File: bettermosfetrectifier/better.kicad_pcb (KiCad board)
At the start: 2 copper layers, 20 parts, among them IC1 LT4322RMS8#PBF, IC2 LT4322RMS8#PBF, IC3 LT4322RMS8#PBF, IC4 LT4322RMS8#PBF, IC5 LT4322RMS8#PBF, IC6 LT4322RMS8#PBF, J1 Conn_01x02, J2 Conn_01x03, Q1 IRFS7430-7P, Q2 IRFS7430-7P, Q3 IRFS7430-7P, Q4 IRFS7430-7P, Q5 IRFS7430-7P, Q6 IRFS7430-7P

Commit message: Add files via upload
Added depletion mode mosfets and added capacitors on power mosfet gates
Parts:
- added C1: 10nF, Capacitor_SMD:C_0603_1608Metric, F.Cu at (90.5, 91.3)
- added C2: 10nF, Capacitor_SMD:C_0603_1608Metric, F.Cu at (90.5, 93.8)
- added C3: 10nF, Capacitor_SMD:C_0603_1608Metric, F.Cu at (90.5, 96.3)
- added C4: 10nF, Capacitor_SMD:C_0603_1608Metric, F.Cu at (90.5, 98.8)
- added C5: 10nF, Capacitor_SMD:C_0603_1608Metric, F.Cu at (90.5, 101.3)
- added C6: 10nF, Capacitor_SMD:C_0603_1608Metric, F.Cu at (90.5, 103.8)
- added Q10: DN3135, Library:SOT-89_3MC_MCH, F.Cu at (104.1, 76.4)
- added Q11: DN3135, Library:SOT-89_3MC_MCH, F.Cu at (110.4, 76.4)
- added Q12: DN3135, Library:SOT-89_3MC_MCH, F.Cu at (116.7, 76.4)
- added Q7: DN3135, Library:SOT-89_3MC_MCH, F.Cu at (104.0, 70.5)
- added Q8: DN3135, Library:SOT-89_3MC_MCH, F.Cu at (110.2, 70.5)
- added Q9: DN3135, Library:SOT-89_3MC_MCH, F.Cu at (116.5, 70.5)
- CVDDA1, CVDDA2, CVDDA3, CVDDA4, CVDDA5, CVDDA6: footprint Capacitor_SMD:C_0201_0603Metric -> Capacitor_SMD:C_0603_1608Metric
- moved Q1 46.1 mm to (72.4, 49.0), turned to 0 degrees
- moved Q6 30.1 mm to (70.9, 104.5)
- moved CVDDA2 28.8 mm to (90.7, 65.0)
- moved CVDDA1 26.9 mm to (90.8, 69.5)
- moved Q2 26.5 mm to (72.0, 35.5), turned to 0 degrees
- moved Q5 23.7 mm to (71.0, 91.0)
- moved Q4 17.1 mm to (71.4, 77.5)
- moved CVDDA6 11.6 mm to (90.5, 85.5)
- moved Q3 11.1 mm to (71.8, 63.5)
- moved CVDDA5 8.01 mm to (90.5, 82.0)
- moved CVDDA4 3.39 mm to (90.7, 78.0)
- moved IC3 2.42 mm to (98.8, 49.4)
- moved IC4 2.42 mm to (98.8, 54.0)
- moved IC5 2.42 mm to (98.8, 58.7)
- moved IC6 2.42 mm to (98.8, 63.3)
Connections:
- CVDDA2 pad 1: Net-(IC1-CATHODE) -> Net-(J2-Pin_1)
- CVDDA3 pad 1: Net-(IC4-CATHODE) -> Net-(J2-Pin_2)
- CVDDA5 pad 1: Net-(IC6-CATHODE) -> Net-(J2-Pin_3)
- IC3 pad 5: Net-(IC2-CATHODE) -> Net-(IC3-CATHODE)
- IC3 pad 8: Net-(IC2-CATHODE) -> Net-(IC3-CATHODE)
- IC5 pad 5: Net-(IC2-CATHODE) -> Net-(IC5-CATHODE)
- IC5 pad 8: Net-(IC2-CATHODE) -> Net-(IC5-CATHODE)
- J1 pad 1: Net-(IC2-CATHODE) -> Net-(J1-Pin_1)
- J2 pad 1: Net-(IC1-CATHODE) -> Net-(J2-Pin_1)
- J2 pad 2: Net-(IC4-CATHODE) -> Net-(J2-Pin_2)
- J2 pad 3: Net-(IC6-CATHODE) -> Net-(J2-Pin_3)
- Q1 pad 4: Net-(IC1-CATHODE) -> Net-(J2-Pin_1)
- Q2 pad 2: Net-(IC1-CATHODE) -> Net-(J2-Pin_1)
- Q2 pad 3: Net-(IC1-CATHODE) -> Net-(J2-Pin_1)
- Q2 pad 4: Net-(IC2-CATHODE) -> Net-(J1-Pin_1)
- Q2 pad 5: Net-(IC1-CATHODE) -> Net-(J2-Pin_1)
- Q2 pad 6: Net-(IC1-CATHODE) -> Net-(J2-Pin_1)
- Q3 pad 2: Net-(IC4-CATHODE) -> Net-(J2-Pin_2)
- Q3 pad 3: Net-(IC4-CATHODE) -> Net-(J2-Pin_2)
- Q3 pad 4: Net-(IC2-CATHODE) -> Net-(J1-Pin_1)
- Q3 pad 5: Net-(IC4-CATHODE) -> Net-(J2-Pin_2)
- Q3 pad 6: Net-(IC4-CATHODE) -> Net-(J2-Pin_2)
- Q4 pad 4: Net-(IC4-CATHODE) -> Net-(J2-Pin_2)
- Q5 pad 2: Net-(IC6-CATHODE) -> Net-(J2-Pin_3)
- Q5 pad 3: Net-(IC6-CATHODE) -> Net-(J2-Pin_3)
- Q5 pad 4: Net-(IC2-CATHODE) -> Net-(J1-Pin_1)
- Q5 pad 5: Net-(IC6-CATHODE) -> Net-(J2-Pin_3)
- Q5 pad 6: Net-(IC6-CATHODE) -> Net-(J2-Pin_3)
- Q6 pad 4: Net-(IC6-CATHODE) -> Net-(J2-Pin_3)

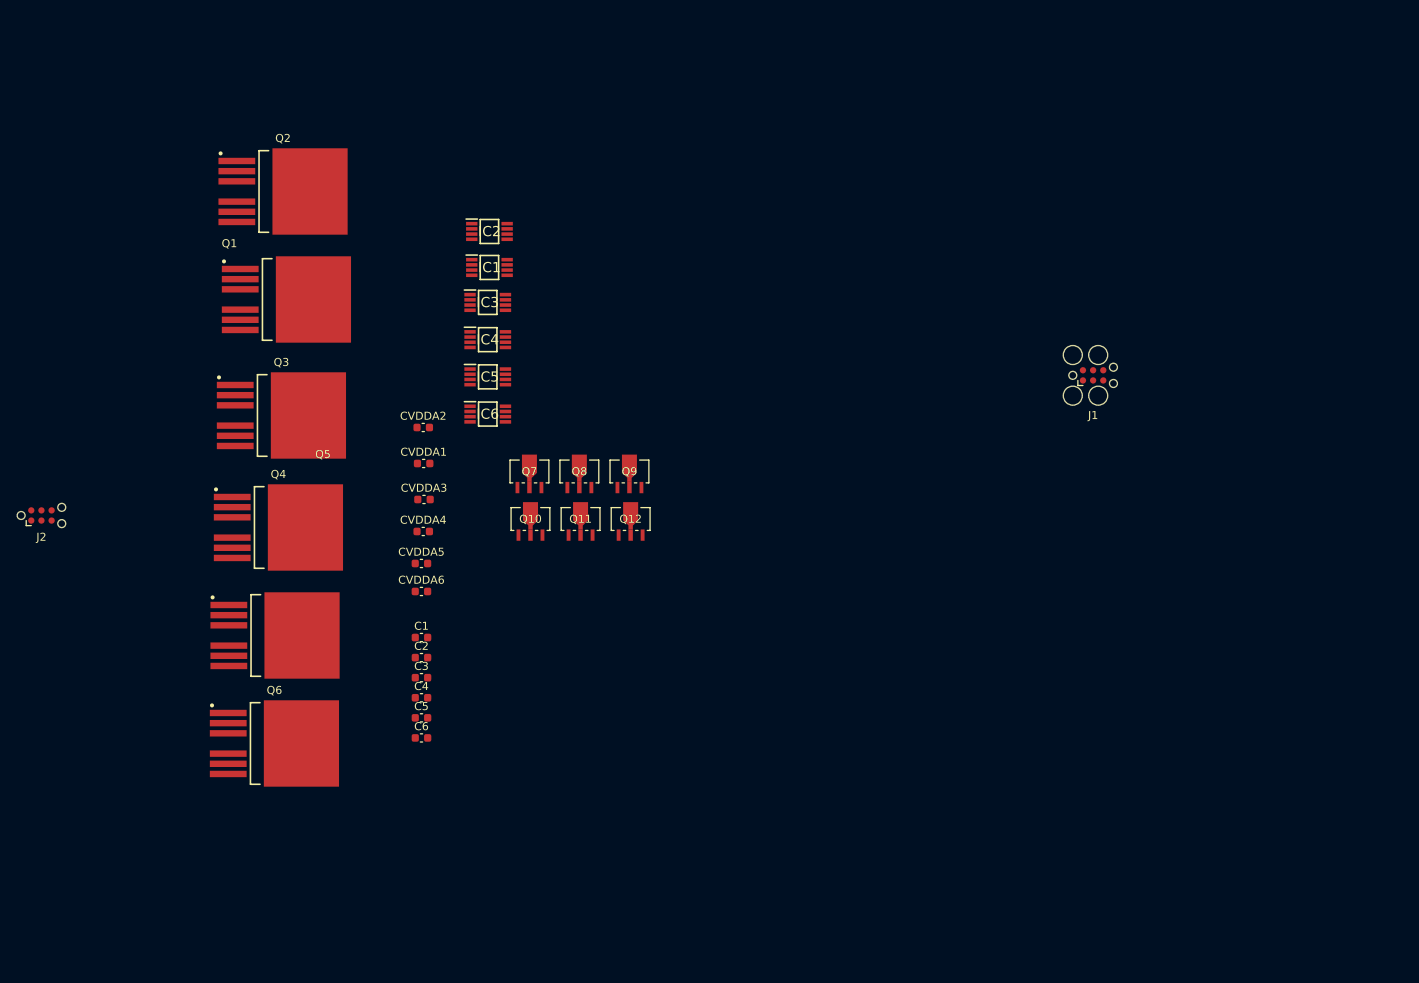
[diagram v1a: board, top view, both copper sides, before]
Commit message: Goon
Changed mosfets to 100V 16A ones (old ones were 40V 240A), added footprints to capacitors and terminals
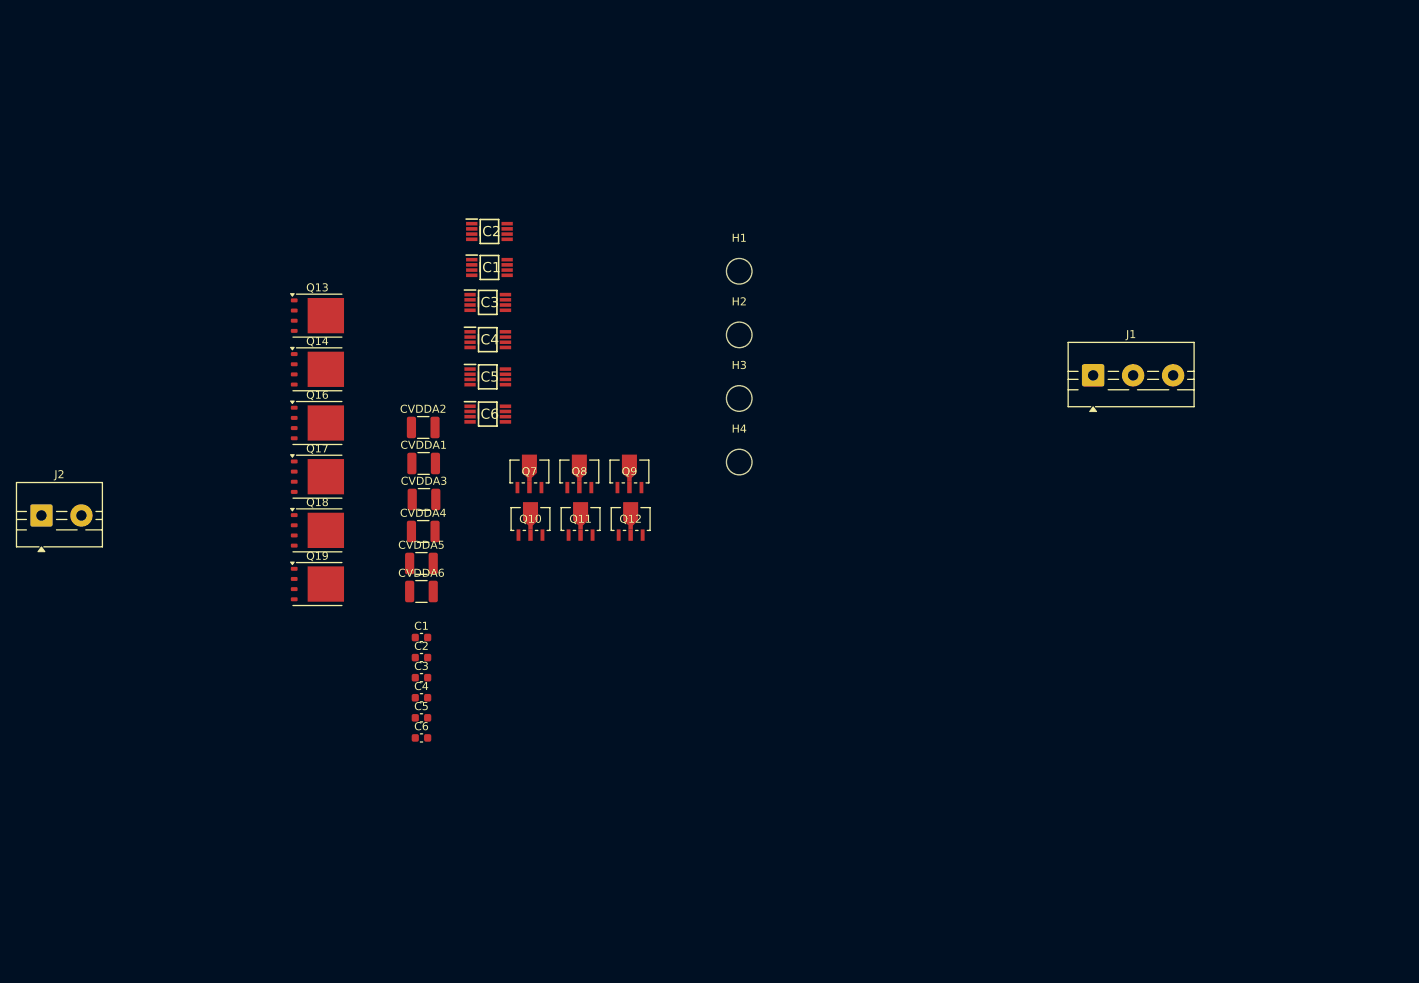
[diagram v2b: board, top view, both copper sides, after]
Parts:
- removed Q1, Q2, Q3, Q4, Q5, Q6: IRFS7430-7P, TO127P1524X508-8_7N-V1:TO127P1524X508-8_7N
- added H1: MountingHole, MountingHole:MountingHole_3.2mm_M3, F.Cu at (130.2, 45.5)
- added H2: MountingHole, MountingHole:MountingHole_3.2mm_M3, F.Cu at (130.2, 53.4)
- added H3: MountingHole, MountingHole:MountingHole_3.2mm_M3, F.Cu at (130.2, 61.4)
- added H4: MountingHole, MountingHole:MountingHole_3.2mm_M3, F.Cu at (130.2, 69.3)
- added Q13: BSC050N10NS5ATMA1, Package_TO_SOT_SMD:TDSON-8-1, F.Cu at (77.5, 51.0)
- added Q14: BSC050N10NS5ATMA1, Package_TO_SOT_SMD:TDSON-8-1, F.Cu at (77.5, 57.7)
- added Q16: BSC050N10NS5ATMA1, Package_TO_SOT_SMD:TDSON-8-1, F.Cu at (77.5, 64.4)
- added Q17: BSC050N10NS5ATMA1, Package_TO_SOT_SMD:TDSON-8-1, F.Cu at (77.5, 71.2)
- added Q18: BSC050N10NS5ATMA1, Package_TO_SOT_SMD:TDSON-8-1, F.Cu at (77.5, 77.9)
- added Q19: BSC050N10NS5ATMA1, Package_TO_SOT_SMD:TDSON-8-1, F.Cu at (77.5, 84.6)
- CVDDA1, CVDDA2, CVDDA3, CVDDA4, CVDDA5, CVDDA6: footprint Capacitor_SMD:C_0603_1608Metric -> Capacitor_SMD:C_1210_3225Metric
- J1: footprint Connector:Tag-Connect_TC2030-IDC-FP_2x03_P1.27mm_Vertical -> TerminalBlock:TerminalBlock_MaiXu_MX126-5.0-03P_1x03_P5.00mm
- J2: footprint Connector:Tag-Connect_TC2030-IDC-NL_2x03_P1.27mm_Vertical -> TerminalBlock:TerminalBlock_MaiXu_MX126-5.0-02P_1x02_P5.00mm
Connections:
- C1 pad 2: Net-(J2-Pin_1) -> Net-(IC2-ANODE)
- C2 pad 1: Net-(J1-Pin_2) -> Net-(IC1-ANODE)
- C3 pad 2: Net-(J2-Pin_2) -> Net-(IC3-ANODE)
- C4 pad 1: Net-(J1-Pin_2) -> Net-(IC1-ANODE)
- C5 pad 2: Net-(J2-Pin_3) -> Net-(IC5-ANODE)
- C6 pad 1: Net-(J1-Pin_2) -> Net-(IC1-ANODE)
- CVDDA1 pad 1: Net-(J1-Pin_2) -> Net-(IC1-ANODE)
- CVDDA2 pad 1: Net-(J2-Pin_1) -> Net-(IC2-ANODE)
- CVDDA3 pad 1: Net-(J2-Pin_2) -> Net-(IC3-ANODE)
- CVDDA4 pad 1: Net-(J1-Pin_2) -> Net-(IC1-ANODE)
- CVDDA5 pad 1: Net-(J2-Pin_3) -> Net-(IC5-ANODE)
- CVDDA6 pad 1: Net-(J1-Pin_2) -> Net-(IC1-ANODE)
- IC4 pad 2: Net-(IC4-ANODE) -> Net-(IC1-ANODE)
- IC4 pad 3: Net-(IC4-ANODE) -> Net-(IC1-ANODE)
- IC6 pad 2: Net-(IC6-ANODE) -> Net-(IC1-ANODE)
- IC6 pad 3: Net-(IC6-ANODE) -> Net-(IC1-ANODE)
- J1 pad 2: Net-(J1-Pin_2) -> Net-(IC1-ANODE)
- J2 pad 1: Net-(J2-Pin_1) -> Net-(IC2-ANODE)
- J2 pad 2: Net-(J2-Pin_2) -> Net-(IC3-ANODE)
- Q10 pad 2: Net-(J2-Pin_1) -> Net-(IC2-ANODE)
- Q11 pad 2: Net-(J2-Pin_2) -> Net-(IC3-ANODE)
- Q12 pad 2: Net-(J2-Pin_3) -> Net-(IC5-ANODE)

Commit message: Add more capacitance
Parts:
- J1: footprint TerminalBlock:TerminalBlock_MaiXu_MX126-5.0-03P_1x03_P5.00mm -> TerminalBlock:TerminalBlock_MaiXu_MX126-5.0-02P_1x02_P5.00mm
- J2: footprint TerminalBlock:TerminalBlock_MaiXu_MX126-5.0-02P_1x02_P5.00mm -> TerminalBlock:TerminalBlock_MaiXu_MX126-5.0-03P_1x03_P5.00mm
- moved J2 105.4 mm to (146.0, 54.0), turned to -90 degrees
- moved Q13 93.3 mm to (170.4, 42.6)
- moved C1 90.0 mm to (180.5, 92.7)
- moved C2 90.0 mm to (180.5, 95.2)
- moved C3 90.0 mm to (180.5, 97.7)
- moved C4 90.0 mm to (180.5, 100.2)
- moved C5 90.0 mm to (180.5, 102.7)
- moved C6 90.0 mm to (180.5, 105.2)
- moved CVDDA1 88.7 mm to (175.3, 96.5)
- moved CVDDA2 88.7 mm to (175.2, 92.0)
- moved CVDDA3 88.7 mm to (175.3, 101.0)
- moved CVDDA4 88.7 mm to (175.2, 105.0)
- moved CVDDA5 88.7 mm to (175.0, 109.0)
- moved CVDDA6 88.7 mm to (175.0, 112.5)
- moved Q14 86.8 mm to (158.7, 88.5)
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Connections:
- net Net-(IC1-ANODE) renamed GND
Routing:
- added copper zone on B.Cu, net GND
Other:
- board outline added: 60 x 50 mm

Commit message: made stupid chopped layout :( :( :(
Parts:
- added C10: 220uF, Capacitor_SMD:CP_Elec_6.3x5.4_Nichicon, F.Cu at (183.5, 60.7)
- added C11: 220uF, Capacitor_SMD:CP_Elec_6.3x5.4_Nichicon, F.Cu at (168.3, 77.3)
- added C12: 220uF, Capacitor_SMD:CP_Elec_6.3x5.4_Nichicon, F.Cu at (183.2, 88.5)
- added C7: 220uF, Capacitor_SMD:CP_Elec_6.3x5.4_Nichicon, F.Cu at (168.5, 49.8)
- added C8: 220uF, Capacitor_SMD:CP_Elec_6.3x5.4_Nichicon, F.Cu at (168.0, 22.7)
- added C9: 220uF, Capacitor_SMD:CP_Elec_6.3x5.4_Nichicon, F.Cu at (182.8, 34.0)
- CVDDA1, CVDDA2, CVDDA3, CVDDA4, CVDDA5, CVDDA6: value 10uF -> 0.1uF; footprint Capacitor_SMD:C_1210_3225Metric -> Capacitor_SMD:C_0603_1608Metric
- moved H1 73.9 mm to (192.2, 93.8), turned to 90 degrees
- moved C1 73.4 mm to (177.9, 19.3), turned to 90 degrees
- moved CVDDA2 69.4 mm to (172.6, 22.6), turned to -90 degrees
- moved IC1 63.3 mm to (175.5, 32.5), turned to 90 degrees
- moved H4 63.0 mm to (192.5, 16.8), turned to 90 degrees
- moved CVDDA1 62.4 mm to (178.2, 34.2), turned to 90 degrees
- moved C2 58.2 mm to (173.0, 37.5), turned to 90 degrees
- moved Q16 55.5 mm to (182.9, 45.4)
- moved Q7 54.2 mm to (183.6, 24.9)
- moved C3 51.1 mm to (178.2, 46.7), turned to 90 degrees
- moved CVDDA3 51.0 mm to (173.0, 50.0), turned to -90 degrees
- moved Q9 50.7 mm to (184.0, 79.8)
- moved Q14 50.5 mm to (168.3, 38.9), turned to 180 degrees
- moved IC3 48.6 mm to (176.0, 51.7), turned to -90 degrees
- moved Q8 48.3 mm to (184.0, 52.2)
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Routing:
- net Net-(J1-Pin_1): track 0.00 -> 3.41 mm
- removed copper zone on B.Cu, net GND
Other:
- board outline removed

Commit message: idk improved layout a bit
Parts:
- Q10, Q11, Q12, Q7, Q8, Q9: footprint Library:SOT-89_3MC_MCH -> Package_TO_SOT_SMD:SOT-89-3
- moved H2 25.0 mm to (155.8, 118.0)
- moved H1 24.7 mm to (196.8, 118.0)
- moved C12 18.9 mm to (184.4, 107.5)
- moved CVDDA6 18.9 mm to (179.9, 107.4)
- moved Q18 18.9 mm to (183.9, 91.5)
- moved C5 18.9 mm to (179.2, 92.8)
- moved Q9 18.9 mm to (185.0, 98.6), turned to 0 degrees
- moved C11 18.9 mm to (169.2, 96.2)
- moved IC6 18.9 mm to (176.8, 105.7)
- moved IC5 18.9 mm to (176.8, 97.9)
- moved C6 18.9 mm to (174.1, 110.9)
- moved Q12 18.9 mm to (168.1, 105.2), turned to 180 degrees
- moved Q19 18.9 mm to (169.3, 112.2)
- moved CVDDA5 18.9 mm to (173.8, 96.2)
- moved IC4 17.4 mm to (176.8, 76.3)
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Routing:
- net Net-(J1-Pin_1): track 3.41 -> 0.00 mm
- added copper zone on B.Cu, net GND
- added copper zone on F.Cu, net Net-(J1-Pin_1)
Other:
- board outline added: 48 x 102 mm
